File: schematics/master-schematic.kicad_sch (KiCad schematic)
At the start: 5 parts

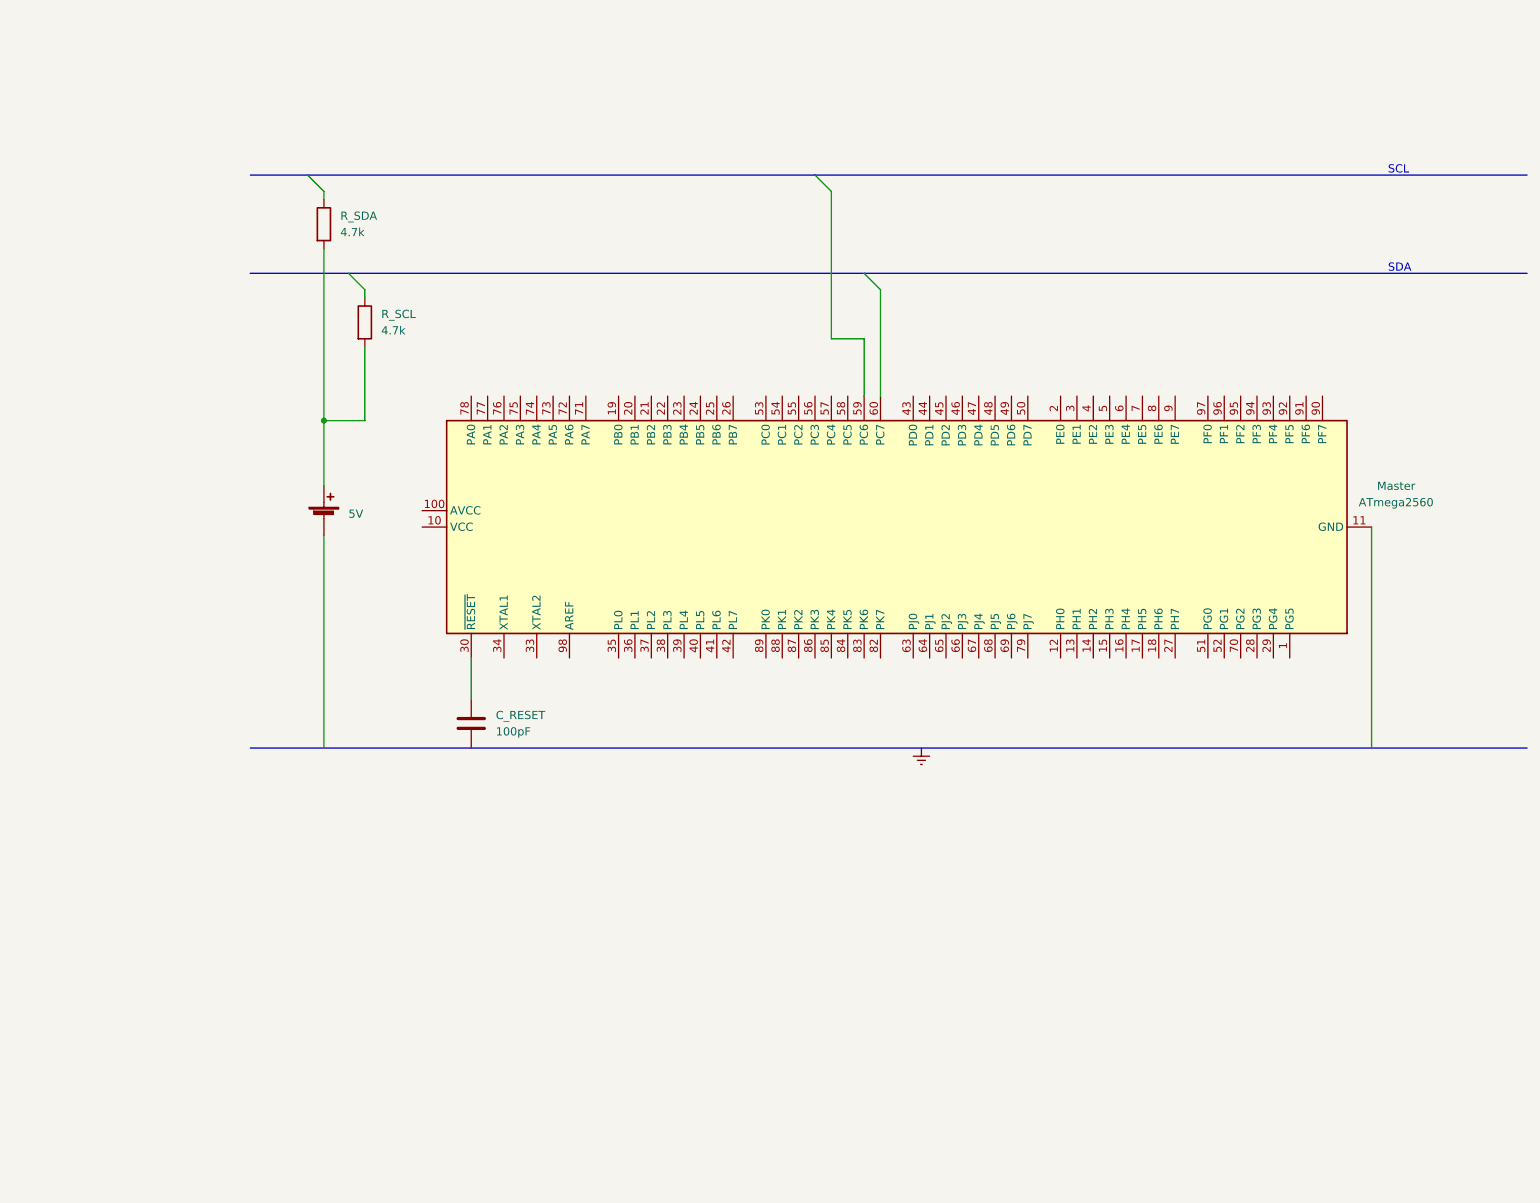
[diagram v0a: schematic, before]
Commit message: Improved schematics and added examination data
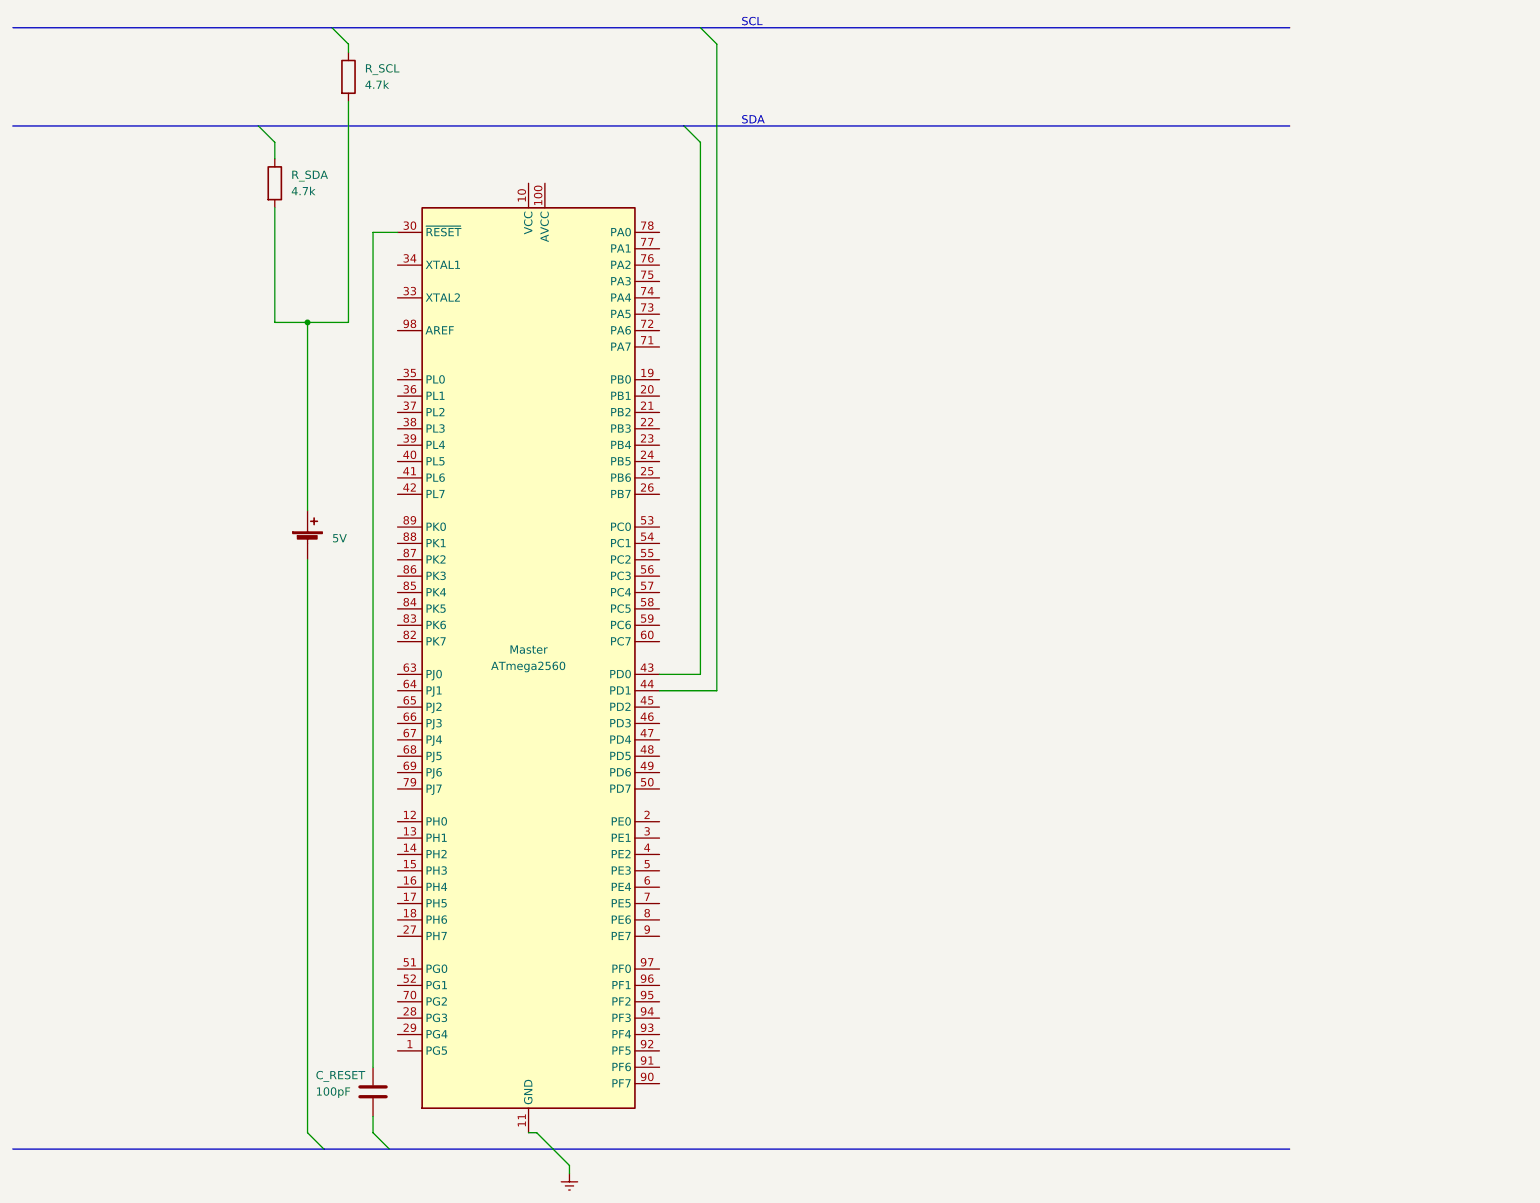
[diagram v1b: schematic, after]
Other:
- moved on the sheet: C_RESET, Master, R_SCL, R_SDA
